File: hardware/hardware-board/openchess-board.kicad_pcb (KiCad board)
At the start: 2 copper layers, 292 x 292 mm, 247 parts, among them J1 Conn_02x13, U1 DRV5032FC, U10 DRV5032FC, U11 DRV5032FC, U12 DRV5032FC, U13 DRV5032FC, U14 DRV5032FC, U15 DRV5032FC, U16 DRV5032FC, U17 DRV5032FC, U18 DRV5032FC, U19 DRV5032FC, U2 DRV5032FC, U20 DRV5032FC, U21 DRV5032FC, U22 DRV5032FC, U23 DRV5032FC, U24 DRV5032FC, U25 DRV5032FC, U26 DRV5032FC, U27 DRV5032FC, U28 DRV5032FC, U29 DRV5032FC, U3 DRV5032FC, U30 DRV5032FC, U31 DRV5032FC, U32 DRV5032FC, U33 DRV5032FC, U34 DRV5032FC, U35 DRV5032FC, U36 DRV5032FC, U37 DRV5032FC, U38 DRV5032FC, U39 DRV5032FC, U4 DRV5032FC, U40 DRV5032FC, U41 DRV5032FC, U42 DRV5032FC, U43 DRV5032FC, U44 DRV5032FC, U45 DRV5032FC, U46 DRV5032FC, U47 DRV5032FC, U48 DRV5032FC, U49 DRV5032FC, U5 DRV5032FC, U50 DRV5032FC, U51 DRV5032FC, U52 DRV5032FC, U53 DRV5032FC, U54 DRV5032FC, U55 DRV5032FC, U56 DRV5032FC, U57 DRV5032FC, U58 DRV5032FC, U59 DRV5032FC, U6 DRV5032FC, U60 DRV5032FC, U61 DRV5032FC, U62 DRV5032FC, U63 DRV5032FC, U64 DRV5032FC, U7 DRV5032FC, U8 DRV5032FC, U9 DRV5032FC

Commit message: Add scripts to merge and tile PDF layers for KiCad projects
- Implemented `merge_pdf_layers.py` to overlay multiple single-page PDFs into one page, allowing for easy printing of layered designs.
- Created `tile_pdf_to_a4.py` to split large PDFs into A4-sized tiles with configurable overlap, facilitating printing on standard home printers.
- Both scripts require the `pypdf` library for PDF manipulation.
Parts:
- removed FID1, FID2, FID3: Fiducial, Fiducial:Fiducial_1mm_Mask2mm
- removed MH1, MH2, MH3, MH4: M3, MountingHole:MountingHole_3.2mm_M3
- removed TP1, TP2, TP3, TP4: TestPoint, TestPoint:TestPoint_Pad_D1.5mm
- moved C40 26.6 mm to (151.2, 145.2)
- moved C41 26.6 mm to (183.2, 145.2)
- moved C42 26.6 mm to (215.2, 145.2)
- moved C43 26.6 mm to (247.2, 145.2)
- moved C44 26.6 mm to (279.2, 145.2)
- moved C45 26.6 mm to (311.2, 145.2)
- moved C49 26.6 mm to (151.2, 177.2)
- moved C50 26.6 mm to (183.2, 177.2)
- moved C51 26.6 mm to (215.2, 177.2)
- moved C52 26.6 mm to (247.2, 177.2)
- moved C53 26.6 mm to (279.2, 177.2)
- moved C54 26.6 mm to (311.2, 177.2)
- moved C58 26.6 mm to (151.2, 209.2)
- moved C59 26.6 mm to (183.2, 209.2)
- moved C60 26.6 mm to (215.2, 209.2)
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
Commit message: Refactor code structure for improved readability and maintainability
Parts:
- added FID1: Fiducial, Fiducial:Fiducial_1mm_Mask2mm, F.Cu at (100.0, 56.0)
- added FID2: Fiducial, Fiducial:Fiducial_1mm_Mask2mm, F.Cu at (262.0, 56.0)
- added FID3: Fiducial, Fiducial:Fiducial_1mm_Mask2mm, F.Cu at (282.0, 326.0)
- added H1: MountingHole, MountingHole:MountingHole_3.2mm_M3, F.Cu at (56.0, 56.0)
- added H2: MountingHole, MountingHole:MountingHole_3.2mm_M3, F.Cu at (326.0, 56.0)
- added H3: MountingHole, MountingHole:MountingHole_3.2mm_M3, F.Cu at (56.0, 326.0)
- added H4: MountingHole, MountingHole:MountingHole_3.2mm_M3, F.Cu at (326.0, 326.0)
- moved C1 23.3 mm to (63.0, 57.4)
- moved C2 23.2 mm to (63.0, 89.1)
- moved C3 23.1 mm to (63.0, 120.8)
- moved C4 23.0 mm to (63.0, 152.6)
- moved C5 22.9 mm to (63.0, 184.3)
- moved C6 22.9 mm to (63.0, 216.1)
- moved C7 22.8 mm to (63.0, 247.8)
- moved C8 22.7 mm to (63.0, 279.6)
- moved C9 22.7 mm to (63.0, 311.4)
- moved D1 20.9 mm to (64.0, 64.0)
- moved U8 20.8 mm to (79.9, 79.9)
- moved D10 20.8 mm to (64.0, 95.8)
- moved D2 20.8 mm to (95.8, 64.0)
- moved C10 20.6 mm to (69.5, 64.0), turned to -90 degrees
- moved D19 20.6 mm to (64.0, 127.5)
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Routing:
- net +5V_LED: track 0.00 -> 2893.9 mm
- net /S7: track 0.00 -> 468.3 mm, vias 0 -> 2
- net /S6: track 0.00 -> 439.6 mm, vias 0 -> 2
- net /S5: track 0.00 -> 404.8 mm, vias 0 -> 2
- net /CA_PWR: track 0.00 -> 398.6 mm, vias 0 -> 10
- net /LED_DATA_5V: track 0.00 -> 383.6 mm, vias 0 -> 2
- net /S4: track 0.00 -> 376.1 mm, vias 0 -> 2
- net /CH_PWR: track 0.00 -> 369.9 mm, vias 0 -> 11
- net /CB_PWR: track 0.00 -> 365.0 mm, vias 0 -> 11
- net /CG_PWR: track 0.00 -> 342.4 mm, vias 0 -> 11
- net /S3: track 0.00 -> 341.3 mm, vias 0 -> 2
- net /CC_PWR: track 0.00 -> 337.6 mm, vias 0 -> 11
- net /S2: track 0.00 -> 312.6 mm, vias 0 -> 2
- net /CF_PWR: track 0.00 -> 308.8 mm, vias 0 -> 11
- net /CD_PWR: track 0.00 -> 304.2 mm, vias 0 -> 11
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- added copper zone on B.Cu, net GND
- added copper zone on F.Cu, net GND
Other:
- board size 292 x 292 mm -> 282 x 282 mm
- board text removed: "WHITE"

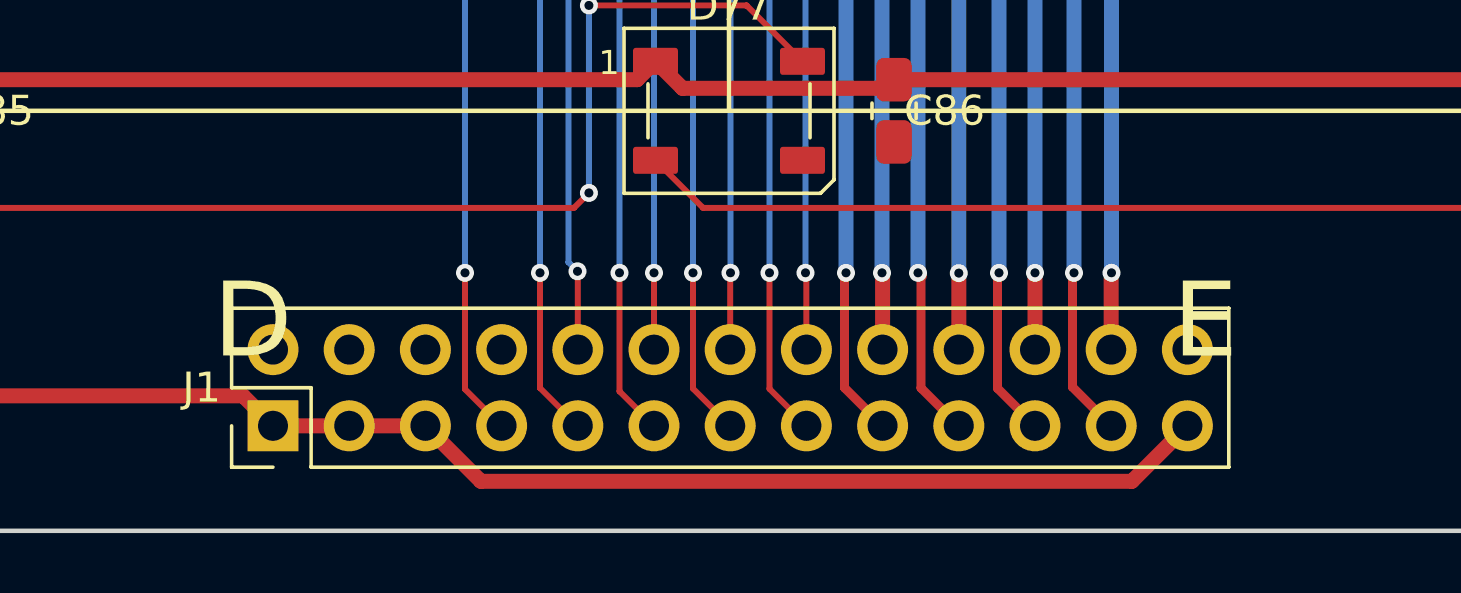
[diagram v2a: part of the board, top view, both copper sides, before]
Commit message: Add JLCPCB BOM and CPL generation scripts for OpenChess board
- Created openchess-board-jlc-bom.csv to define unique components with their specifications for JLCPCB.
- Created openchess-board-jlc-cpl.csv to specify the placement of components on the board.
- Implemented make_jlc_assembly.py script to automate the generation of BOM and CPL from KiCad's exported all-pos.csv.
- The script handles Y-axis flipping and formats output according to JLCPCB requirements.
- Excluded mechanical components from assembly files as per JLCPCB guidelines.
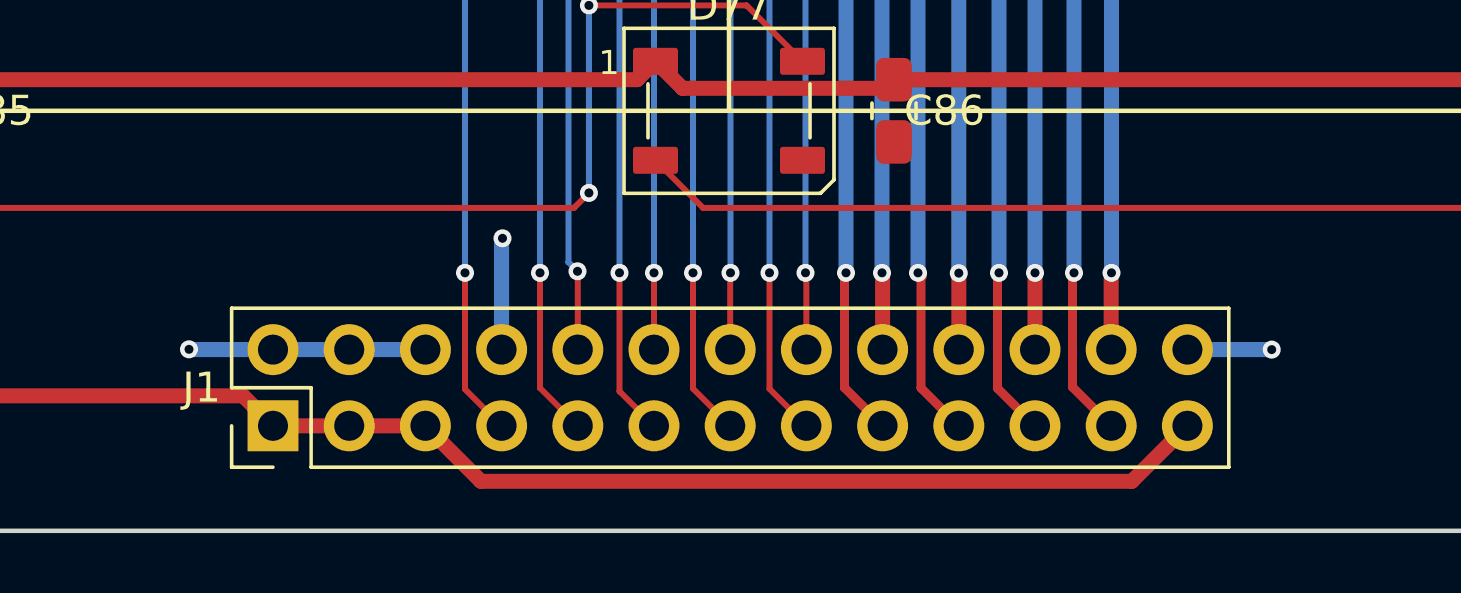
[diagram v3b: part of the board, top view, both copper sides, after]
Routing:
- net GND: track 0.00 -> 14.4 mm, vias 0 -> 3
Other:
- board text removed: "D"
- board text removed: "E"
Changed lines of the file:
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@@
 		(capping no)
 		(filling no)
+		(aux_axis_origin 50 332)
+		(grid_origin 50 332)
 		(pcbplotparams
 			(layerselection 0x00000000_00000000_55555555_5755f5ff)
@@
 			(plotframeref no)
 			(mode 1)
-			(useauxorigin no)
+			(useauxorigin yes)
 			(pdf_front_fp_property_popups yes)
 			(pdf_back_fp_property_popups yes)
@@
 			(crossoutdnponfab yes)
 			(subtractmaskfromsilk no)
-			(outputformat 4)
+			(outputformat 1)
 			(mirror no)
 			(drillshape 0)
 			(scaleselection 1)
-			(outputdirectory "images")
+			(outputdirectory "gerbers")
 		)
 	)
@@
 		)
 	)
-	(gr_text "D"
-		(at 175.125 325 0)
-		(layer "F.SilkS")
-		(effects
-			(font
-				(size 2.5 2.5)
-				(thickness 0.3)
-			)
-		)
-	)
-	(gr_text "E"
-		(at 206.875 325 0)
-		(layer "F.SilkS")
-		(effects
-			(font
-				(size 2.5 2.5)
-				(thickness 0.3)
-			)
-		)
-	)
 	(gr_text "F"
 		(at 238.625 325 0)
@@
 		(net "/CG_PWR")
 	)
+	(via
+		(at 209.09 325.96)
+		(size 0.6)
+		(drill 0.3)
+		(layers "F.Cu" "B.Cu")
+		(net "GND")
+	)
+	(via
+		(at 183.45 322.25)
+		(size 0.6)
+		(drill 0.3)
+		(layers "F.Cu" "B.Cu")
+		(net "GND")
+	)
+	(via
+		(at 173 325.95)
+		(size 0.6)
+		(drill 0.3)
+		(layers "F.Cu" "B.Cu")
+		(net "GND")
+	)
+	(segment
+		(start 183.42 325.96)
+		(end 183.42 322.28)
+		(width 0.5)
+		(layer "B.Cu")
+		(net "GND")
+	)
+	(segment
+		(start 173.01 325.96)
+		(end 173 325.95)
+		(width 0.2)
+		(layer "B.Cu")
+		(net "GND")
+	)
+	(segment
+		(start 180.88 325.96)
+		(end 173.01 325.96)
+		(width 0.5)
+		(layer "B.Cu")
+		(net "GND")
+	)
+	(segment
+		(start 183.42 322.28)
+		(end 183.45 322.25)
+		(width 0.2)
+		(layer "B.Cu")
+		(net "GND")
+	)
+	(segment
+		(start 206.28 325.96)
+		(end 209.09 325.96)
+		(width 0.5)
+		(layer "B.Cu")
+		(net "GND")
+	)
 	(segment

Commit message: Add initial positions CSV for hardware components
This commit introduces a new CSV file containing the designator, midpoints, rotation, and layer information for various hardware components used in the project. The data includes positions for capacitors, resistors, diodes, and connectors, which are essential for the assembly and layout of the hardware.
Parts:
- added R1: 1k, Resistor_SMD:R_0805_2012Metric_Pad1.20x1.40mm_HandSolder, F.Cu at (84.7, 310.1)
- added R2: 1k, Resistor_SMD:R_0805_2012Metric_Pad1.20x1.40mm_HandSolder, F.Cu at (117.5, 308.9)
- added R3: 1k, Resistor_SMD:R_0805_2012Metric_Pad1.20x1.40mm_HandSolder, F.Cu at (150.1, 307.9)
- added R4: 1k, Resistor_SMD:R_0805_2012Metric_Pad1.20x1.40mm_HandSolder, F.Cu at (182.2, 306.4)
- added R5: 1k, Resistor_SMD:R_0805_2012Metric_Pad1.20x1.40mm_HandSolder, F.Cu at (196.9, 305.2)
- added R6: 1k, Resistor_SMD:R_0805_2012Metric_Pad1.20x1.40mm_HandSolder, F.Cu at (230.9, 306.4)
- added R7: 1k, Resistor_SMD:R_0805_2012Metric_Pad1.20x1.40mm_HandSolder, F.Cu at (263.0, 307.9)
- added R8: 1k, Resistor_SMD:R_0805_2012Metric_Pad1.20x1.40mm_HandSolder, F.Cu at (294.6, 308.9)
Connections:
- U1 pad 2: GND -> /S0
- U1 pad 3: /S0 -> GND
- U10 pad 2: GND -> /S1
- U10 pad 3: /S1 -> GND
- U11 pad 2: GND -> /S2
- U11 pad 3: /S2 -> GND
- U12 pad 2: GND -> /S3
- U12 pad 3: /S3 -> GND
- U13 pad 2: GND -> /S4
- U13 pad 3: /S4 -> GND
- U14 pad 2: GND -> /S5
- U14 pad 3: /S5 -> GND
- U15 pad 2: GND -> /S6
- U15 pad 3: /S6 -> GND
- U16 pad 2: GND -> /S7
- U16 pad 3: /S7 -> GND
- U17 pad 2: GND -> /S0
- U17 pad 3: /S0 -> GND
- U18 pad 2: GND -> /S1
- U18 pad 3: /S1 -> GND
- U19 pad 2: GND -> /S2
- U19 pad 3: /S2 -> GND
- U2 pad 2: GND -> /S1
- U2 pad 3: /S1 -> GND
- U20 pad 2: GND -> /S3
- U20 pad 3: /S3 -> GND
- U21 pad 2: GND -> /S4
- U21 pad 3: /S4 -> GND
- U22 pad 2: GND -> /S5
- U22 pad 3: /S5 -> GND
- U23 pad 2: GND -> /S6
- U23 pad 3: /S6 -> GND
- U24 pad 2: GND -> /S7
- U24 pad 3: /S7 -> GND
- U25 pad 2: GND -> /S0
- U25 pad 3: /S0 -> GND
- U26 pad 2: GND -> /S1
- U26 pad 3: /S1 -> GND
- U27 pad 2: GND -> /S2
- U27 pad 3: /S2 -> GND
- U28 pad 2: GND -> /S3
- U28 pad 3: /S3 -> GND
- U29 pad 2: GND -> /S4
- U29 pad 3: /S4 -> GND
- U3 pad 2: GND -> /S2
- U3 pad 3: /S2 -> GND
- U30 pad 2: GND -> /S5
- U30 pad 3: /S5 -> GND
- U31 pad 2: GND -> /S6
- U31 pad 3: /S6 -> GND
- U32 pad 2: GND -> /S7
- U32 pad 3: /S7 -> GND
- U33 pad 2: GND -> /S0
- U33 pad 3: /S0 -> GND
- U34 pad 2: GND -> /S1
- U34 pad 3: /S1 -> GND
- U35 pad 2: GND -> /S2
- U35 pad 3: /S2 -> GND
- U36 pad 2: GND -> /S3
- U36 pad 3: /S3 -> GND
- U37 pad 2: GND -> /S4
- U37 pad 3: /S4 -> GND
- U38 pad 2: GND -> /S5
- U38 pad 3: /S5 -> GND
- U39 pad 2: GND -> /S6
- U39 pad 3: /S6 -> GND
- U4 pad 2: GND -> /S3
- U4 pad 3: /S3 -> GND
- U40 pad 2: GND -> /S7
- U40 pad 3: /S7 -> GND
- U41 pad 2: GND -> /S0
- U41 pad 3: /S0 -> GND
- U42 pad 2: GND -> /S1
- U42 pad 3: /S1 -> GND
- U43 pad 2: GND -> /S2
- U43 pad 3: /S2 -> GND
- U44 pad 2: GND -> /S3
- U44 pad 3: /S3 -> GND
- U45 pad 2: GND -> /S4
- U45 pad 3: /S4 -> GND
- U46 pad 2: GND -> /S5
- U46 pad 3: /S5 -> GND
- U47 pad 2: GND -> /S6
- U47 pad 3: /S6 -> GND
- U48 pad 2: GND -> /S7
- U48 pad 3: /S7 -> GND
- U49 pad 2: GND -> /S0
- U49 pad 3: /S0 -> GND
- U5 pad 2: GND -> /S4
- U5 pad 3: /S4 -> GND
- U50 pad 2: GND -> /S1
- U50 pad 3: /S1 -> GND
- U51 pad 2: GND -> /S2
- U51 pad 3: /S2 -> GND
- U52 pad 2: GND -> /S3
- U52 pad 3: /S3 -> GND
- U53 pad 2: GND -> /S4
- U53 pad 3: /S4 -> GND
- U54 pad 2: GND -> /S5
- U54 pad 3: /S5 -> GND
- U55 pad 2: GND -> /S6
- U55 pad 3: /S6 -> GND
- U56 pad 2: GND -> /S7
- U56 pad 3: /S7 -> GND
- U57 pad 2: GND -> /S0
- U57 pad 3: /S0 -> GND
- U58 pad 2: GND -> /S1
- U58 pad 3: /S1 -> GND
- U59 pad 2: GND -> /S2
- U59 pad 3: /S2 -> GND
- U6 pad 2: GND -> /S5
- U6 pad 3: /S5 -> GND
- U60 pad 2: GND -> /S3
- U60 pad 3: /S3 -> GND
- U61 pad 2: GND -> /S4
- U61 pad 3: /S4 -> GND
- U62 pad 2: GND -> /S5
- U62 pad 3: /S5 -> GND
- U63 pad 2: GND -> /S6
- U63 pad 3: /S6 -> GND
- U64 pad 2: GND -> /S7
- U64 pad 3: /S7 -> GND
- U7 pad 2: GND -> /S6
- U7 pad 3: /S6 -> GND
- U8 pad 2: GND -> /S7
- U8 pad 3: /S7 -> GND
- U9 pad 2: GND -> /S0
- U9 pad 3: /S0 -> GND
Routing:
- net /CE_PWR: track 281.4 -> 284.0 mm, vias 9 -> 10
- net /S1: track 278.1 -> 277.0 mm
- net /S5: track 404.8 -> 403.8 mm
- net /S6: track 439.6 -> 438.7 mm
- net /S4: track 376.1 -> 375.2 mm
- net /S2: track 312.6 -> 311.6 mm
- net /S0: track 249.1 -> 248.2 mm
- net /S7: track 468.3 -> 467.4 mm
- net /S3: track 341.3 -> 340.3 mm
- net GND: vias 3 -> 7
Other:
- board text added: "Matrix Board"
- board text removed: "OpenChess — Matrix Board"
